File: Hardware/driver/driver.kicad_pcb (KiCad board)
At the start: 4 copper layers, 128.1 x 184.5 mm, 134 parts, among them J201 Conn_02x10_Odd_Even, J301 1017526, J401 TBP02R2W-381-03BE, J402 Conn_01x02_Male, M201 Fan_4pin, Q201 MMBT3904, Q202 PN2222A, Q301 IXTH80N075L2, Q302 IXTH80N075L2, U101 ICL7660, U102 DS2482-100, U201 AT24CS32-SSHM, U202 ADUM1250, U203 FODM214, U204 EMC2101-R, U205 NCP716BCSN330T1G, U301 MCP3421A2T-ECH, U302 MCP3421A1T-ECH, U303 DAC60501Z, U304 DAC60501Z, U305 DS18B20, U306 DS18B20, U307 MCP3421A3T-ECH, U308 OPA2388, U309 OPA2388, U310 LM431SC, U311 LM431SC

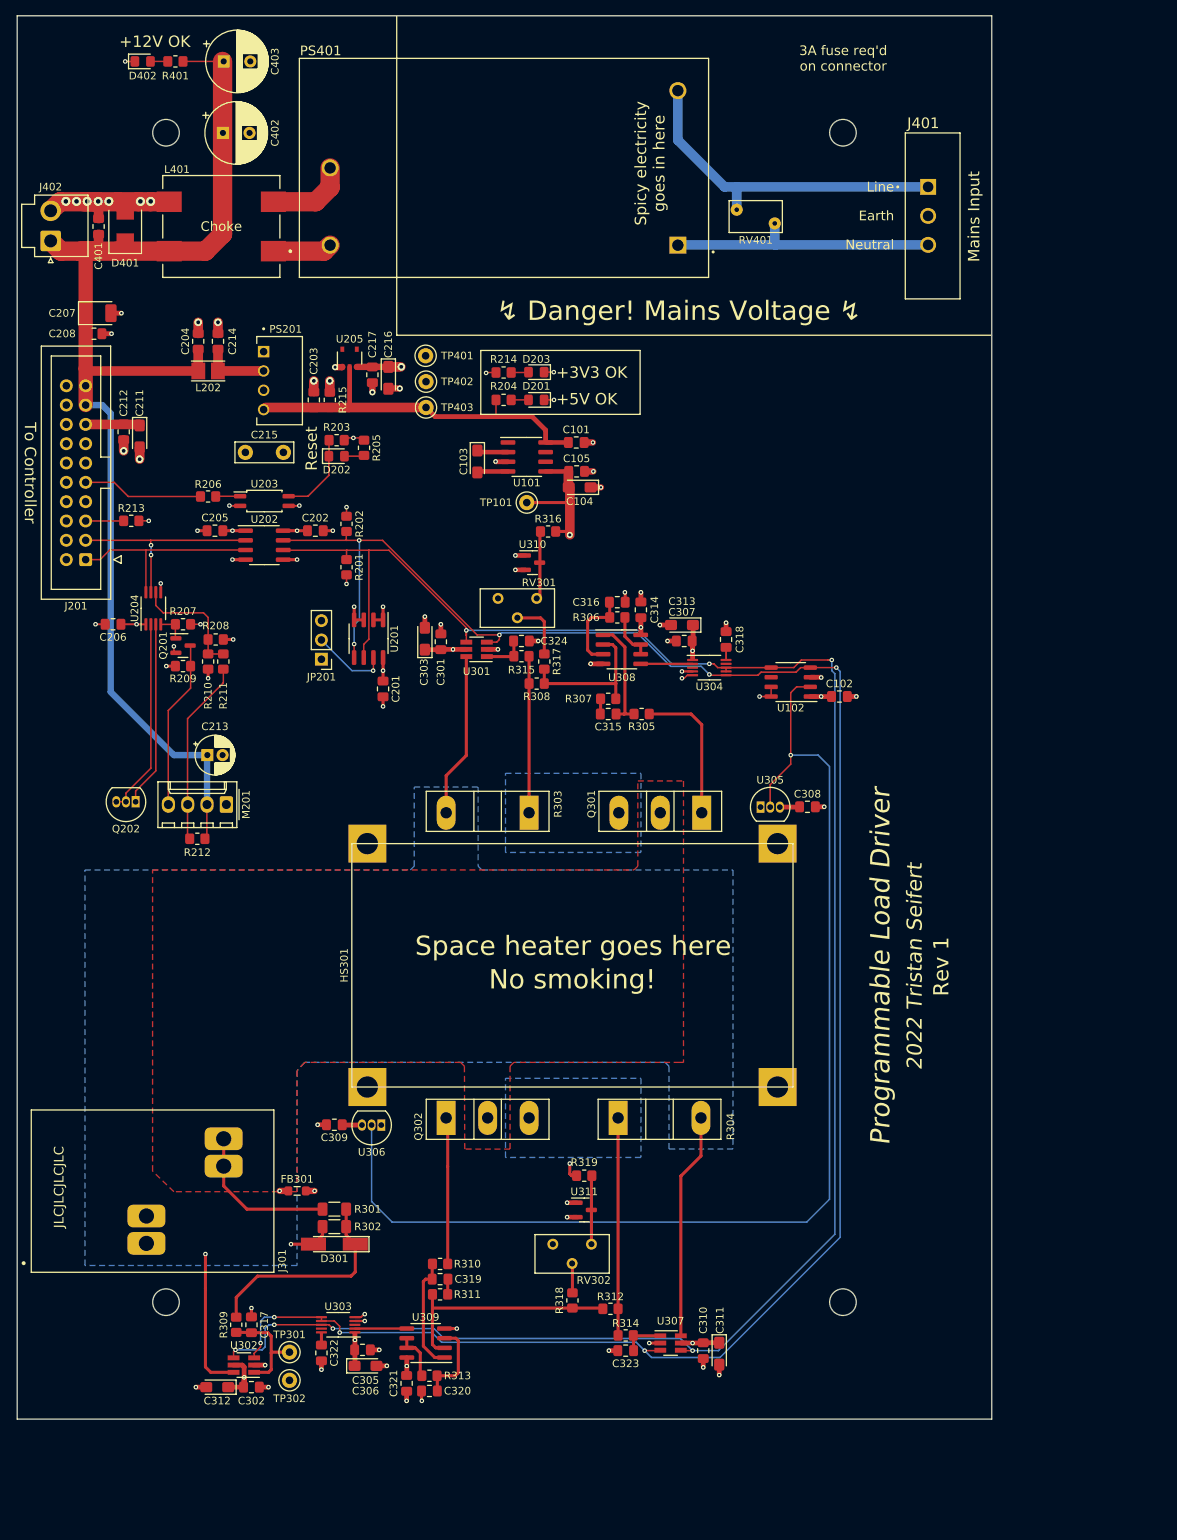
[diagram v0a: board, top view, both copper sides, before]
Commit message: External trigger input
- Added a basic Schmitt-trigger based external trigger input. There's a
  basic pulse shaping circuit attached to it, before its fed into the
  buffer, and then off to the main board to use as an interrupt line to
  control the system mode.
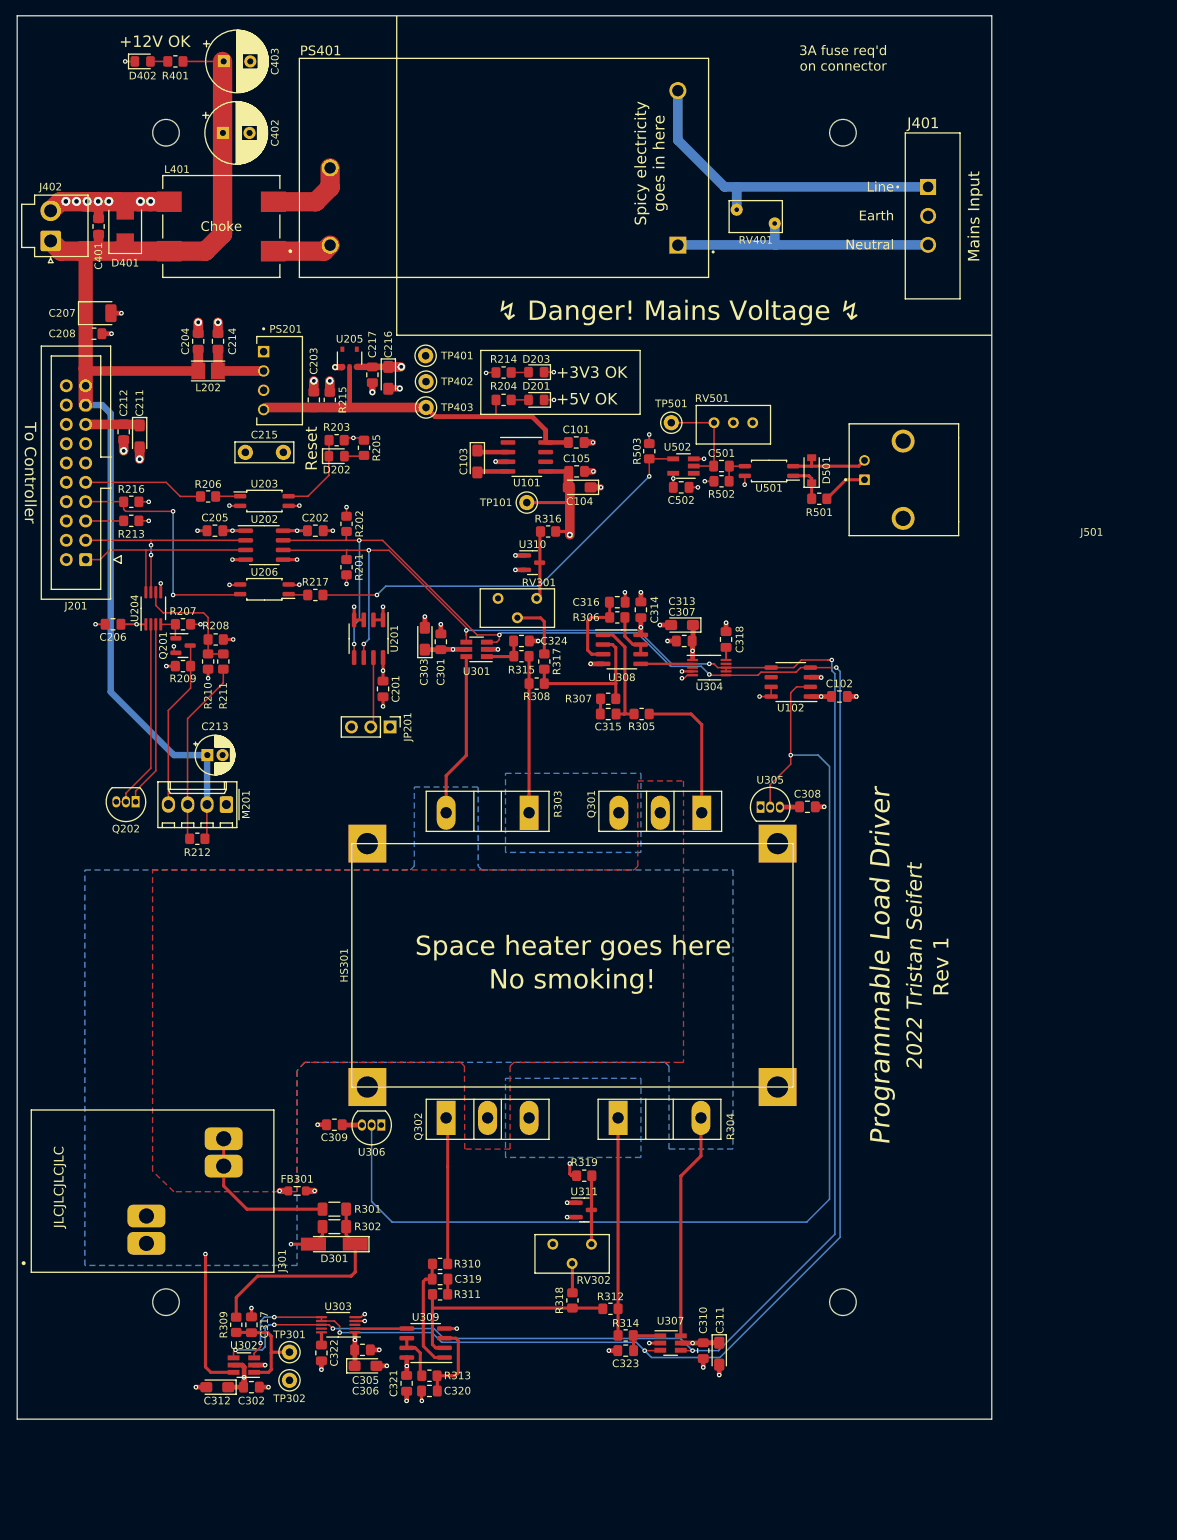
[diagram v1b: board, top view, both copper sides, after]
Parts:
- added C501: 1µF, Capacitor_SMD:C_0805_2012Metric_Pad1.18x1.45mm_HandSolder, F.Cu at (112.6, 79.2)
- added C502: 100nF, Capacitor_SMD:C_0805_2012Metric_Pad1.18x1.45mm_HandSolder, F.Cu at (107.3, 82.0)
- added D501: 1N4148W, Diode_SMD:D_SOD-123, F.Cu at (124.5, 79.8)
- added J501: Conn_Coaxial, programmable-load:CONN_1-1337543-0, F.Cu at (131.4, 81.0)
- added R216: 2k2, Resistor_SMD:R_0805_2012Metric_Pad1.20x1.40mm_HandSolder, F.Cu at (35.0, 83.9)
- added R217: 1k, Resistor_SMD:R_0805_2012Metric_Pad1.20x1.40mm_HandSolder, F.Cu at (59.2, 96.2)
- added R501: 100R, Resistor_SMD:R_0805_2012Metric_Pad1.20x1.40mm_HandSolder, F.Cu at (125.5, 83.5)
- added R502: 47k, Resistor_SMD:R_0805_2012Metric_Pad1.20x1.40mm_HandSolder, F.Cu at (112.6, 81.2)
- added R503: 10k, Resistor_SMD:R_0805_2012Metric_Pad1.20x1.40mm_HandSolder, F.Cu at (103.1, 77.2)
- added RV501: 500k, programmable-load:Potentiometer_Nidec_Copal_CT94EW, F.Cu at (109.1, 71.2)
- added TP501: Trigger, TestPoint:TestPoint_Keystone_5000-5004_Miniature, F.Cu at (106.0, 73.5)
- added U206: FODM217B, Package_SO:SOP-4_4.4x2.6mm_P1.27mm, F.Cu at (52.5, 95.4)
- added U501: FODM217B, Package_SO:SOP-4_4.4x2.6mm_P1.27mm, F.Cu at (118.8, 79.8)
- added U502: 74LVC1G17, Package_TO_SOT_SMD:SOT-23-5_HandSoldering, F.Cu at (107.6, 79.2)
- U203: value FODM214 -> FODM217B
- moved JP201 12.7 mm to (69.0, 113.5), turned to -90 degrees
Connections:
- J201 pad 7: /External Interface/~{ACTIVE} -> /External Interface/~{EXT_TRIG}
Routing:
- net /TRIGGER: track 0.00 -> 55.3 mm, vias 0 -> 2
- net /External Interface/~{EXT_TRIG}: track 0.00 -> 32.4 mm, vias 0 -> 2
- net Net-(RV501-Pad3): track 0.00 -> 14.0 mm
- net Net-(J501-Pad2): track 0.00 -> 10.8 mm
- net GND: track 77.6 -> 83.9 mm, vias 53 -> 58
- net Net-(J501-Pad1): track 0.00 -> 5.99 mm
- net Net-(R501-Pad1): track 0.00 -> 5.21 mm
- net Net-(U501-Pad3): track 0.00 -> 4.05 mm
- net +3V3: track 60.4 -> 63.5 mm, vias 17 -> 19
- net Net-(R217-Pad1): track 0.00 -> 2.52 mm
- net -5V: track 105.8 -> 103.6 mm
- net GNDA: track 42.6 -> 44.0 mm, vias 21 -> 22
- net +3V3A: track 18.5 -> 19.8 mm, vias 6 -> 7
- net Net-(JP201-Pad2): track 10.2 -> 9.27 mm, vias 1 -> 0
- net /I2C_SDA: vias 7 -> 9

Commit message: Start work on remote VSense; driver board tweaks
- Use the DAC reference as the positive end of the null adjustment
  trimmers, rather than the +3V3 supply; this should make the adjustment
  actually useful and persistent rather than relying on the relationship
  between the 3V3 rail and the DAC's internal reference.

- Moved the 1Wire controller slightly to allow relocating the zero
  offset trimmer for the first channel

- Start work on remote VSense

  This works by selecting between either voltage sensing at the source
  terminals, or an external sense input connected to another set of
  terminals. These are switched by a latching relay (as to provide
  satisfying clicky noises) and then go into an op amp working as a
  differential amplifier; it performs a 50:1 gain (obviating the need
  for resistor dividers, and providing greater accuracy) and that then
  goes into the measurement ADC as normal.

  We have to still figure out how to drive the relay (probably just an
  IO expander?) and place those components on the board.
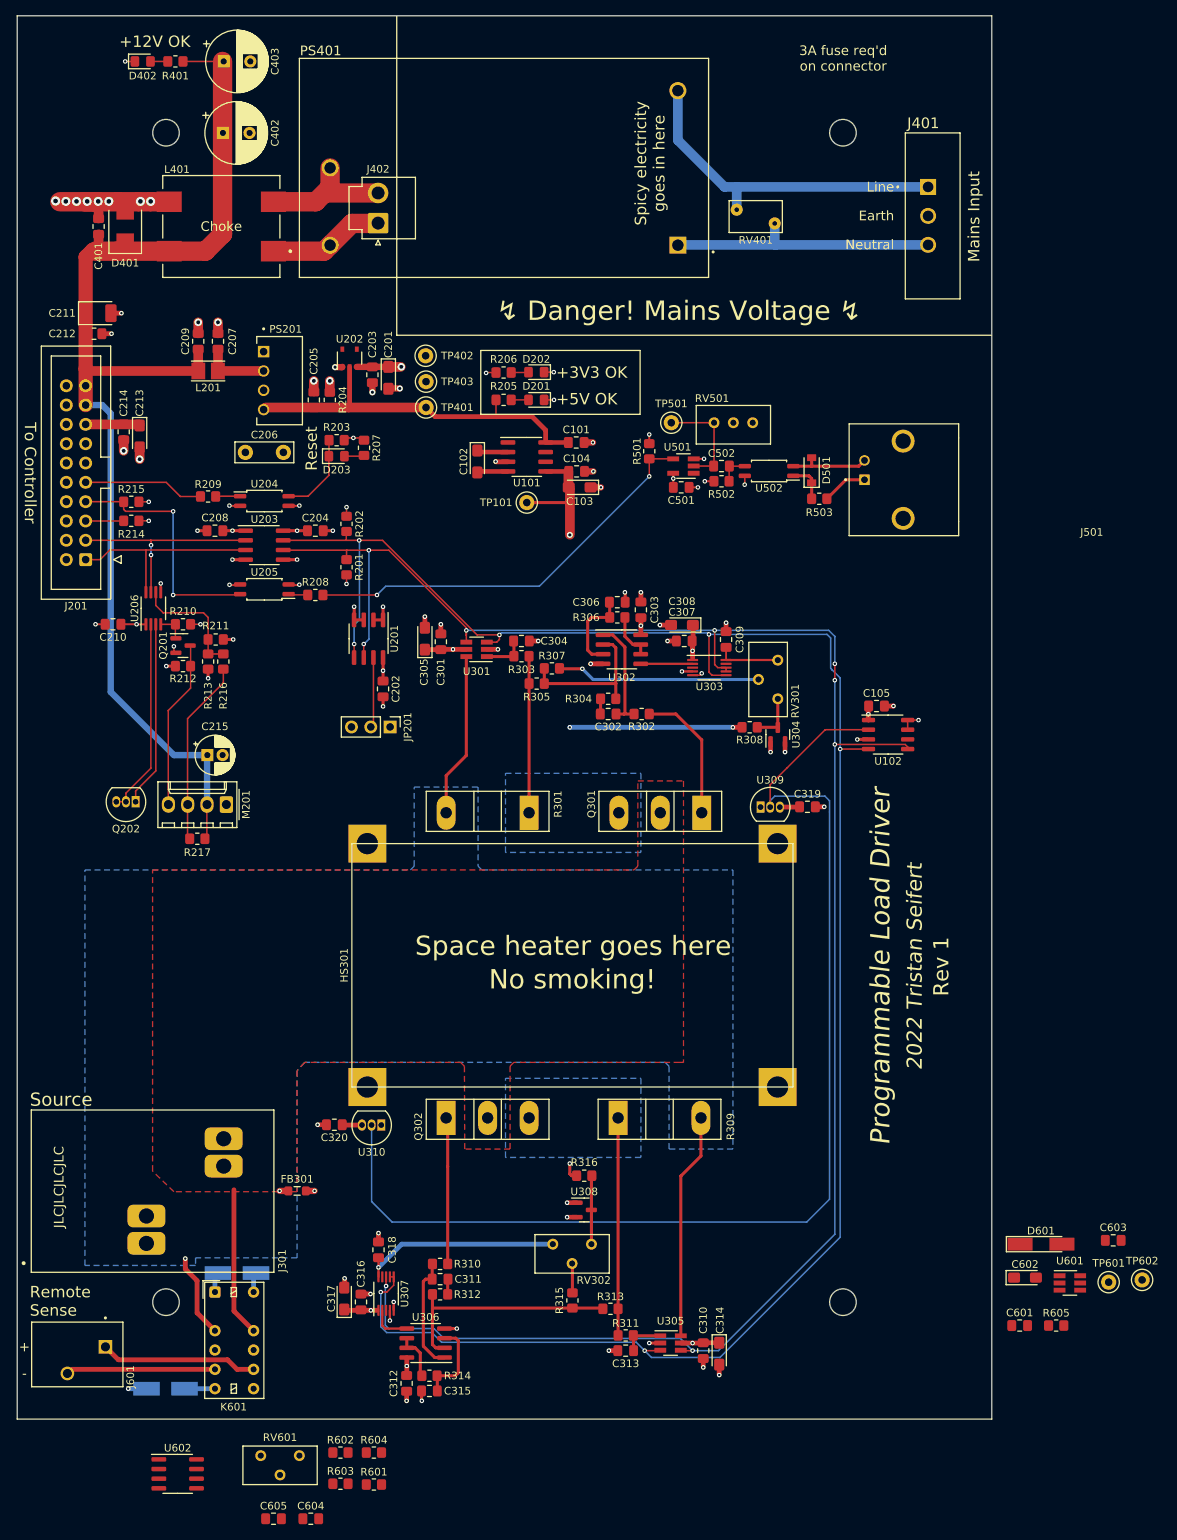
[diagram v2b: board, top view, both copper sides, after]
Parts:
- removed the C302 at (50.8, 200.3)
- removed the C312 at (46.3, 200.3)
- removed the C317 at (50.8, 192.1)
- removed D301: 2V4, Diode_SMD:D_MiniMELF_Handsoldering
- removed the R301 at (61.7, 176.9)
- removed the R302 at (61.7, 179.2)
- removed the R309 at (48.8, 192.1)
- removed TP301: VSense, TestPoint:TestPoint_Keystone_5000-5004_Miniature
- removed TP302: GND, TestPoint:TestPoint_Keystone_5000-5004_Miniature
- removed the U302 at (49.8, 197.4)
- added C601: 100nF, Capacitor_SMD:C_0805_2012Metric_Pad1.18x1.45mm_HandSolder, F.Cu at (151.8, 192.2)
- added C602: 10µF, Capacitor_Tantalum_SMD:CP_EIA-3216-18_Kemet-A_Pad1.58x1.35mm_HandSolder, F.Cu at (152.5, 185.9)
- added C603: 100nF, Capacitor_SMD:C_0805_2012Metric_Pad1.18x1.45mm_HandSolder, F.Cu at (164.1, 181.0)
- added C604: 100nF, Capacitor_SMD:C_0805_2012Metric_Pad1.18x1.45mm_HandSolder, F.Cu at (58.6, 217.6)
- added C605: 100nF, Capacitor_SMD:C_0805_2012Metric_Pad1.18x1.45mm_HandSolder, F.Cu at (53.7, 217.6)
- added D601: 2V4, Diode_SMD:D_MiniMELF_Handsoldering, F.Cu at (154.6, 181.5)
- added D602: SM4007, Diode_SMD:D_SMA_Handsoldering, B.Cu at (48.9, 185.3)
- added D603: SM4007, Diode_SMD:D_SMA_Handsoldering, B.Cu at (39.5, 200.5)
- added J601: Screw_Terminal_01x02, programmable-load:CUI_TBL002A-350-02GR-2OR, F.Cu at (31.6, 195.0)
- added K601: EC2-5TNU, Relay_THT:Relay_DPDT_Kemet_EC2_DoubleCoil, F.Cu at (46.0, 187.8)
- added R601: 1M .1%, Resistor_SMD:R_0805_2012Metric_Pad1.20x1.40mm_HandSolder, F.Cu at (66.9, 213.1)
- added R602: 1M .1%, Resistor_SMD:R_0805_2012Metric_Pad1.20x1.40mm_HandSolder, F.Cu at (62.5, 208.9)
- added R603: 20k .1%, Resistor_SMD:R_0805_2012Metric_Pad1.20x1.40mm_HandSolder, F.Cu at (62.5, 213.0)
- added R604: 20k .1%, Resistor_SMD:R_0805_2012Metric_Pad1.20x1.40mm_HandSolder, F.Cu at (66.9, 208.9)
- added R605: 4k99, Resistor_SMD:R_0805_2012Metric_Pad1.20x1.40mm_HandSolder, F.Cu at (156.6, 192.2)
- added RV601: 20k, programmable-load:Potentiometer_Nidec_Copal_CT94EY, F.Cu at (57.1, 209.3)
- added TP601: VSense+, TestPoint:TestPoint_Keystone_5000-5004_Miniature, F.Cu at (163.5, 186.5)
- added TP602: VSense-, TestPoint:TestPoint_Keystone_5000-5004_Miniature, F.Cu at (167.9, 186.2)
- added U601: MCP3421A1T-ECH, Package_TO_SOT_SMD:SOT-23-6_Handsoldering, F.Cu at (158.4, 186.6)
- added U602: OPA277, Package_SO:SOIC-8_3.9x4.9mm_P1.27mm, F.Cu at (41.1, 211.7)
- moved J402 43.1 mm to (67.5, 47.3)
- moved U304 39.4 mm to (120.0, 114.5), turned to 90 degrees
- moved R308 36.9 mm to (116.3, 113.5), turned to 180 degrees
- moved RV301 34.3 mm to (120.0, 109.8), turned to -90 degrees
- moved C318 15.5 mm to (67.5, 182.2), turned to 90 degrees
- moved U102 14.5 mm to (134.5, 114.5), turned to 0 degrees
- moved C317 9.28 mm to (63.0, 188.7), turned to 90 degrees
- moved U307 7.52 mm to (68.5, 188.0), turned to 90 degrees
- moved C316 6.30 mm to (65.2, 189.1), turned to 90 degrees
- moved C105 5.04 mm to (133.0, 110.8)
- moved R307 1.35 mm to (90.3, 105.8), turned to 180 degrees
- renumbered C103 to C102, C104 to C103, C105 to C104, C102 to C105, C216 to C201, C201 to C202, C217 to C203, C202 to C204, C203 to C205, C215 to C206, C214 to C207, C205 to C208, C204 to C209, C206 to C210, C207 to C211, C208 to C212, C211 to C213, C212 to C214, C213 to C215, C315 to C302, C314 to C303, C324 to C304, C303 to C305, C316 to C306, C313 to C308, C318 to C309, C319 to C311, C321 to C312, C323 to C313, C311 to C314, C320 to C315, C305 to C316, C306 to C317, C322 to C318, C308 to C319, C309 to C320, C502 to C501, C501 to C502, D203 to D202, D202 to D203, L202 to L201, R215 to R204, R204 to R205, R214 to R206, R205 to R207, R217 to R208, R206 to R209, R207 to R210, R208 to R211, R209 to R212, R210 to R213, R213 to R214, R216 to R215, R211 to R216, R212 to R217, R303 to R301, R305 to R302, R315 to R303, R307 to R304, R308 to R305, R317 to R307, R316 to R308, R304 to R309, R314 to R311, R311 to R312, R312 to R313, R313 to R314, R318 to R315, R319 to R316, R503 to R501, R501 to R503, TP403 to TP401, TP401 to TP402, TP402 to TP403, U205 to U202, U202 to U203, U203 to U204, U206 to U205, U204 to U206, U308 to U302, U304 to U303, U310 to U304, U307 to U305, U309 to U306, U303 to U307, U311 to U308, U305 to U309, U306 to U310, U502 to U501, U501 to U502
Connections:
- C309 pad 1: Net-(C318-Pad1) -> /Input Stage/VREF0
- C318 pad 1: Net-(C322-Pad1) -> /Input Stage/VREF1
- J402 pad 1: +12VA -> Net-(J402-Pad1)
- J402 pad 2: GNDA -> Net-(J402-Pad2)
- L401 pad 1: Net-(L401-Pad1) -> Net-(J402-Pad1)
- L401 pad 2: Net-(L401-Pad2) -> Net-(J402-Pad2)
- PS401 pad 3: Net-(L401-Pad2) -> Net-(J402-Pad2)
- PS401 pad 4: Net-(L401-Pad1) -> Net-(J402-Pad1)
- RV301 pad 3: +3V3 -> /Input Stage/VREF0
- RV302 pad 3: +3V3 -> /Input Stage/VREF1
- U303 pad 10: Net-(C318-Pad1) -> /Input Stage/VREF0
- U307 pad 10: Net-(C322-Pad1) -> /Input Stage/VREF1
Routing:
- net Net-(D301-Pad1): track 28.4 -> 0.00 mm
- net /Input Stage/VREF1: track 0.00 -> 26.1 mm, vias 0 -> 1
- net -5V: track 103.6 -> 124.5 mm, vias 2 -> 4
- net /Input Stage/Voltage Sense/SENSE+: track 0.00 -> 20.7 mm
- net /Input Stage/Voltage Sense/SENSE-: track 0.00 -> 19.6 mm
- net Net-(R307-Pad1): track 7.99 -> 26.7 mm, vias 0 -> 1
- net Net-(J402-Pad2): track 0.00 -> 17.2 mm
- net Net-(J402-Pad1): track 0.00 -> 15.3 mm
- net /Input Stage/VSENSE: track 14.0 -> 0.00 mm
- net GNDPWR: track 77.1 -> 63.6 mm, vias 3 -> 2
- net Net-(L401-Pad2): track 10.8 -> 0.00 mm
- net /Input Stage/VREF0: track 0.00 -> 8.46 mm
- net +3V3: track 63.5 -> 55.2 mm, vias 19 -> 18
- net Net-(L401-Pad1): track 7.78 -> 0.00 mm
- net +12VA: track 163.3 -> 155.9 mm
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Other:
- board text added: "+"
- board text added: "-"
- board text added: "Remote Sense"
- board text added: "Source"
